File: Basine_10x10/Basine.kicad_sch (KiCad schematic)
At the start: 28 parts, among them J1 2060-451/998-404, J10 2060-451/998-404, J11 2060-451/998-404, J12 2060-451/998-404, J13 2060-451/998-404, J14 2060-451/998-404, J15 2060-451/998-404, J16 2060-451/998-404, J2 2060-451/998-404, J3 2060-451/998-404, J4 2060-451/998-404, J5 2060-451/998-404, J6 2060-451/998-404, J7 2060-451/998-404, J8 2060-451/998-404, J9 2060-451/998-404

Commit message: Basine_10x10 :
ajout ultrogothe
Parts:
- added JP10, JP11, JP12, JP13, JP14, JP15, JP16, JP5, JP6, JP7, JP8, JP9: SolderJumper_2_Open, Jumper:SolderJumper-2_P1.3mm_Open_TrianglePad1.0x1.5mm, symbol Jumper:SolderJumper_2_Open
- added TP1, TP10, TP11, TP12, TP2, TP3, TP4, TP5, TP6, TP7, TP8, TP9: TestPoint, Chimere_comps:Pastille, symbol Connector:TestPoint
- added U2: ~, symbol Chimere_mods:Ultrogothe
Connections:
- net 0V: now also U2.19 (0V)
- net 3V3: now also U2.20 (3V3)
- net 5V: now also U2.21 (5V)
- net at U7.4 (IO_i): now also JP7.2 (B), TP3.1
- net at U12.4 (IO_i): now also JP12.2 (B), TP8.1
- net at U9.4 (IO_i): now also JP9.2 (B), TP5.1
- net at U5.4 (IO_i): now also JP5.2 (B), TP1.1
- net at U10.4 (IO_i): now also JP10.2 (B), TP6.1
- net at U13.4 (IO_i): now also JP13.2 (B), TP9.1
- net at U6.4 (IO_i): now also JP6.2 (B), TP2.1
- net at U14.4 (IO_i): now also JP14.2 (B), TP10.1
- net at U8.4 (IO_i): now also JP8.2 (B), TP4.1
- net at U16.4 (IO_i): now also JP16.2 (B), TP12.1
- net at U15.4 (IO_i): now also JP15.2 (B), TP11.1
- net at U11.4 (IO_i): now also JP11.2 (B), TP7.1
- no-connect marks 0 -> 10
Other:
- removed sheet s_ALIM_3V3
- note removed: "Ultrogothe"

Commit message: Basine_10x10
ajout symbole ultrogothe
ajout power flag sur 5V
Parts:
- added JP17, JP18: SolderJumper_2_Open, Jumper:SolderJumper-2_P1.3mm_Open_TrianglePad1.0x1.5mm, symbol Jumper:SolderJumper_2_Open
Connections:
- net CAN_RX: now also JP18.2 (B)
- net CAN_TX: now also JP17.2 (B)
- net B0: now reaches JP8.1 (A)
- net B0: now also U2.30 (B0)
- net at U2.14 (B8): now also JP18.1 (A)
- net at U2.15 (B9): now also JP17.1 (A)
- net A0: now reaches U2.22 (A0)
- net A0: now also JP16.1 (A)
- net A1: now reaches U2.23 (A1)
- net A1: now also JP15.1 (A)
- net A2: now reaches U2.24 (A2)
- net A2: now also JP14.1 (A)
- net A3: now reaches U2.25 (A3)
- net A3: now also JP13.1 (A)
- net A4: now reaches U2.26 (A4)
- net A4: now also JP12.1 (A)
- net A5: now reaches U2.27 (A5)
- net A5: now also JP11.1 (A)
- net A6: now reaches U2.28 (A6)
- net A6: now also JP10.1 (A)
- net A7: now reaches U2.29 (A7)
- net A7: now also JP9.1 (A)
- net B1: now reaches U2.31 (B1)
- net B1: now also JP7.1 (A)
- net B2: now reaches U2.32 (B2)
- net B2: now also JP6.1 (A)
- net B10: now reaches U2.33 (B10)
- net B10: now also JP5.1 (A)
- no-connect marks 10 -> 31
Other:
- moved on the sheet: J1, J2, J3, J4, U2

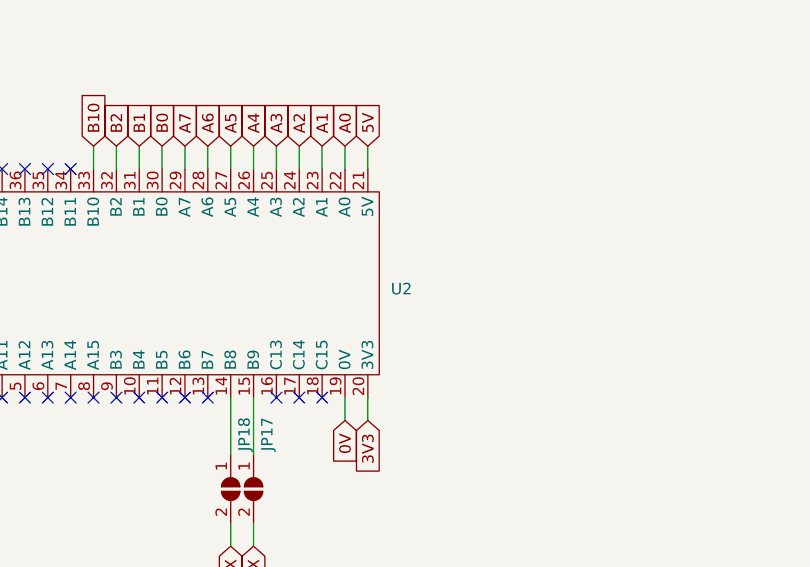
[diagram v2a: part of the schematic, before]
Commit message: 10x10
 ajout empreinte ultrogothe
placement ultrogothe et un peu alim 5V
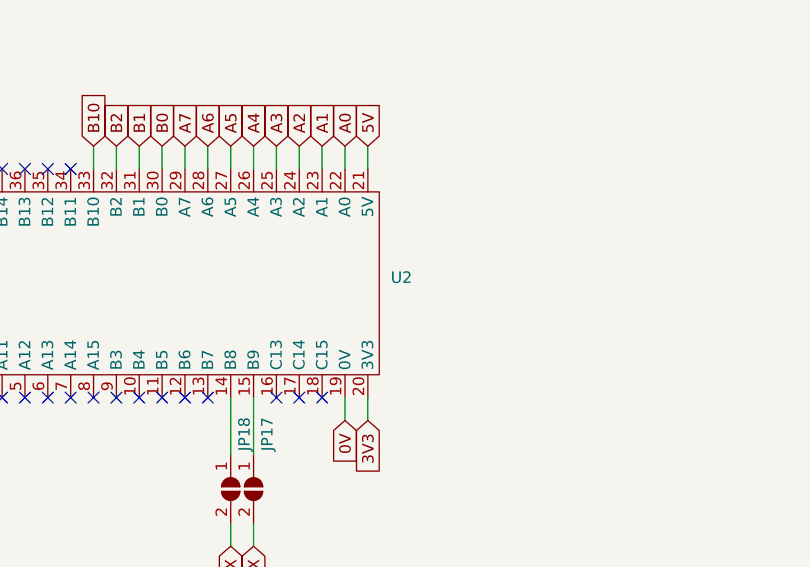
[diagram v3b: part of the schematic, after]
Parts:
- U2: footprint (none) -> Chimere_mods:Ultrogothe
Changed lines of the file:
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@@
 		(fields_autoplaced yes)
 		(property "Reference" "U2"
-			(at 147.32 140.3351 90)
+			(at 147.32 139.0649 90)
 			(effects
 				(font
@@
 		)
 		(property "Value" "~"
-			(at 147.32 138.43 90)
+			(at 147.32 140.97 90)
 			(effects
 				(font
@@
 			)
 		)
-		(property "Footprint" ""
+		(property "Footprint" "Chimere_mods:Ultrogothe"
 			(at 120.65 124.46 0)
 			(effects

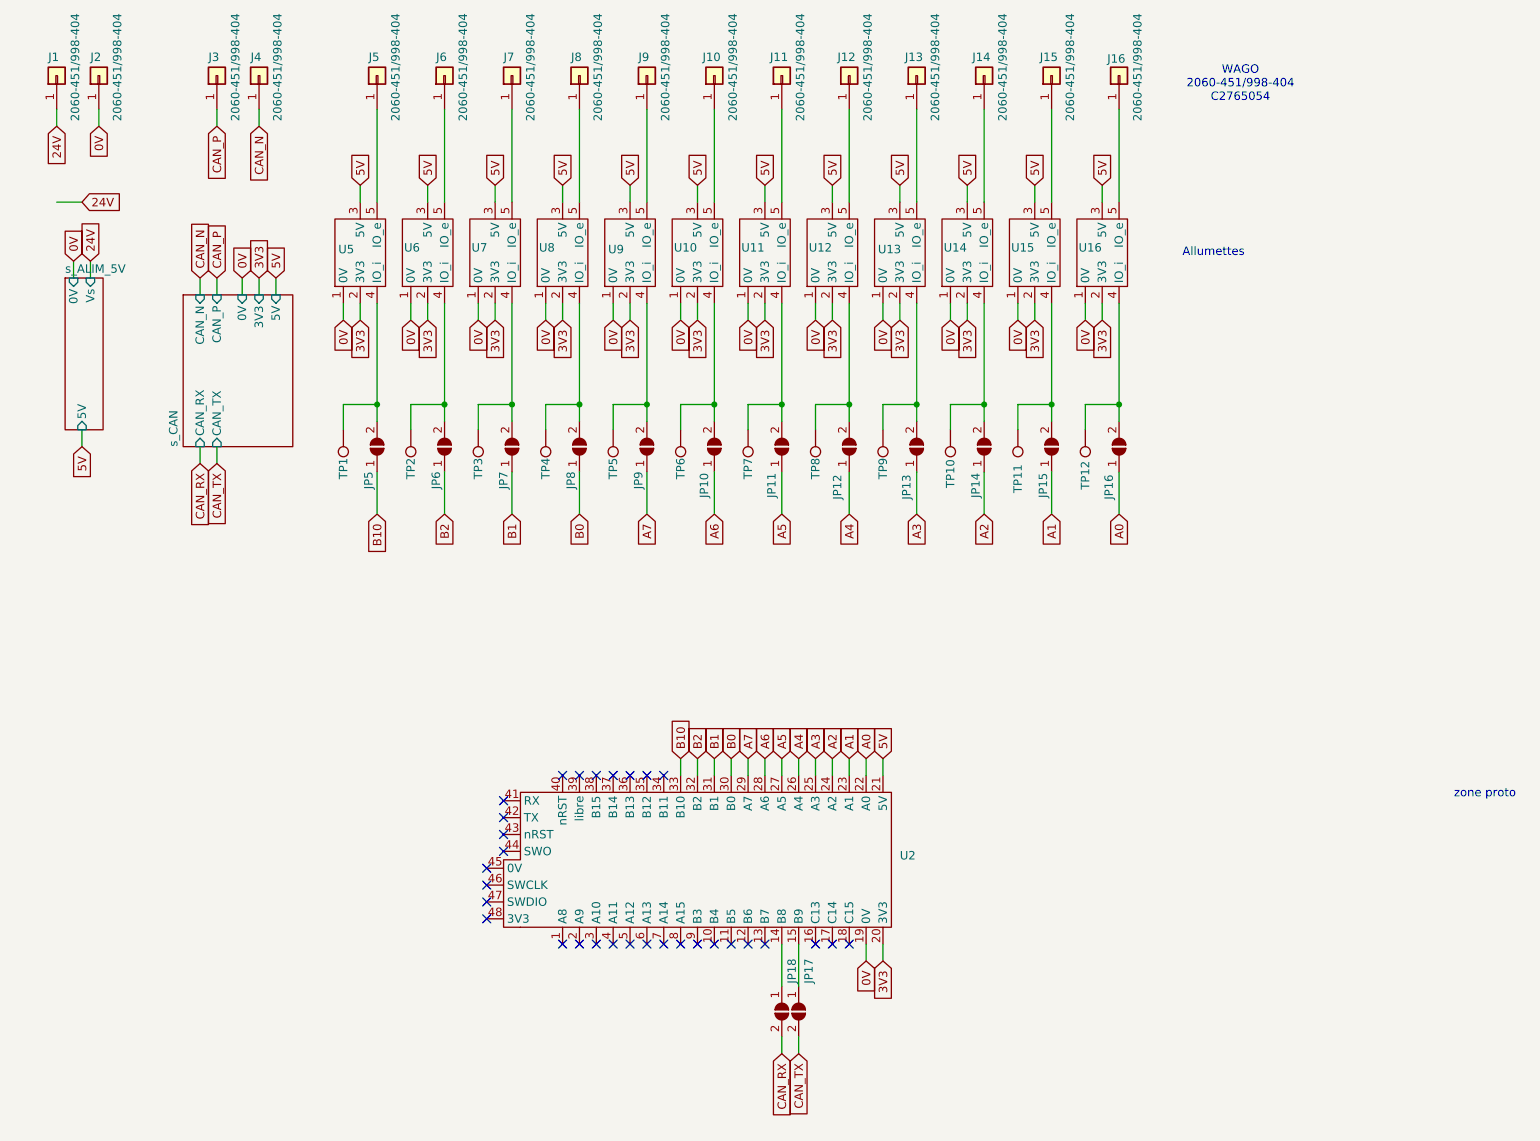
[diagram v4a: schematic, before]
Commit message: 10x10
alim 5V ok
placement et routage ok
reste vias à placer
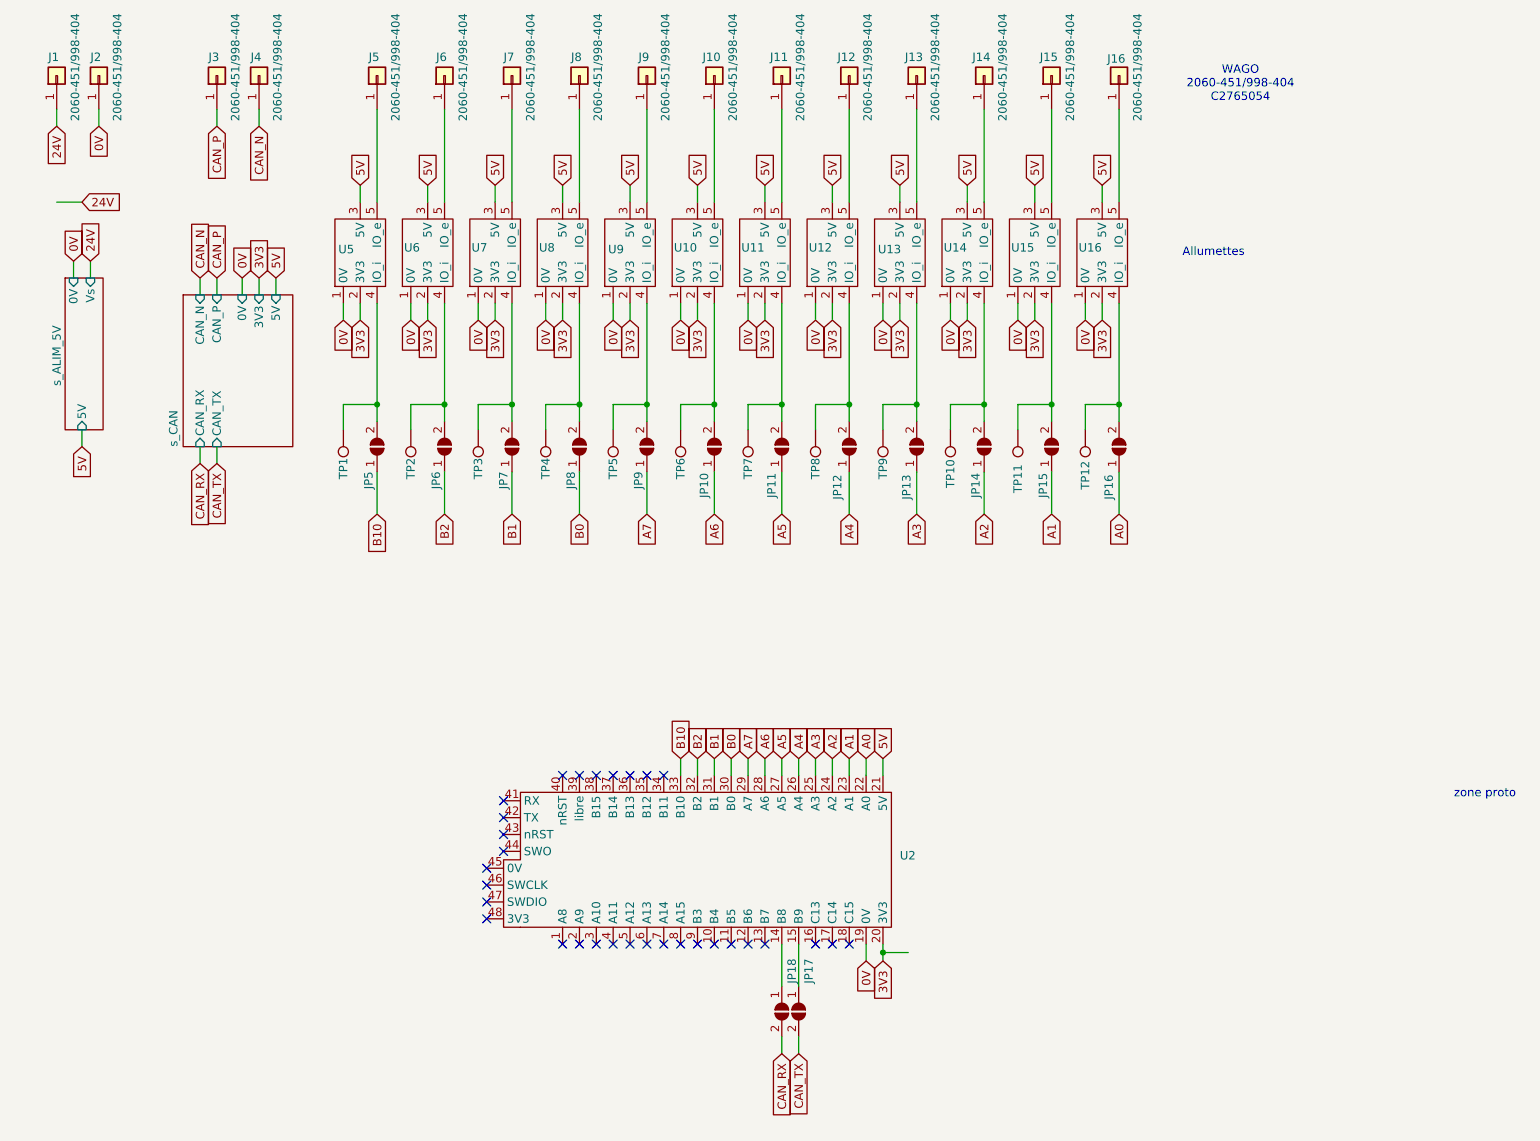
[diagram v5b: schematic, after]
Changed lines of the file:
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@@
 	)
 	(junction
+		(at 144.78 153.67)
+		(diameter 0)
+		(color 0 0 0 0)
+	)
+	(junction
 		(at 170.18 71.12)
 		(diameter 0)
@@
 	(wire
 		(pts
+			(xy 144.78 153.67) (xy 148.59 153.67)
+		)
+		(stroke
+			(width 0)
+			(type default)
+		)
+	)
+	(wire
+		(pts
 			(xy 48.26 52.07) (xy 48.26 54.61)
 		)
@@
 	(wire
 		(pts
+			(xy 144.78 153.67) (xy 144.78 152.4)
+		)
+		(stroke
+			(width 0)
+			(type default)
+		)
+	)
+	(wire
+		(pts
 			(xy 134.62 71.12) (xy 139.7 71.12)
 		)
@@
 	(wire
 		(pts
-			(xy 144.78 154.94) (xy 144.78 152.4)
+			(xy 144.78 154.94) (xy 144.78 153.67)
 		)
 		(stroke
@@
 	(netclass_flag ""
 		(length 2.54)
+		(shape round)
+		(at 148.59 153.67 0)
+		(fields_autoplaced yes)
+		(effects
+			(font
+				(size 1.27 1.27)
+			)
+			(justify left bottom)
+		)
+		(property "Netclass" "alim"
+			(at 149.2885 151.13 0)
+			(effects
+				(font
+					(size 1.27 1.27)
+					(italic yes)
+				)
+				(justify left)
+			)
+		)
+	)
+	(netclass_flag ""
+		(length 2.54)
 		(shape dot)
 		(at 88.9 31.75 90)
@@
 		)
 		(property "Sheetname" "s_ALIM_5V"
-			(at 21.59 51.435 0)
+			(at 21.082 68.326 90)
 			(effects
 				(font

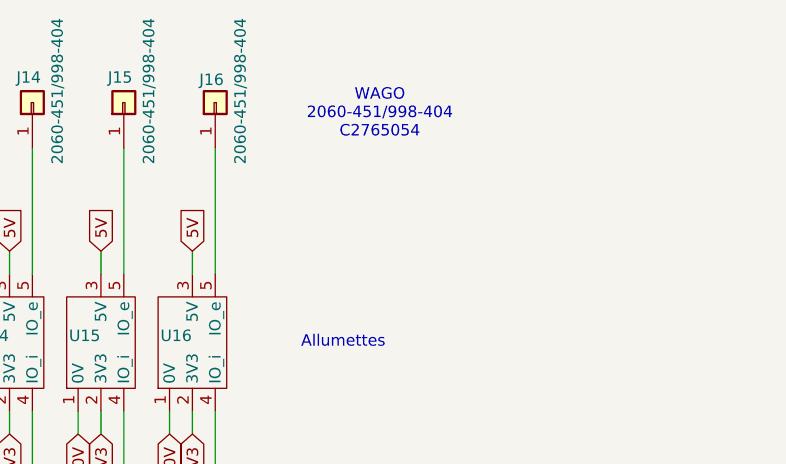
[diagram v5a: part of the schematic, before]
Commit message: 10x10
tentative de fabrication
pénurie spring clamp à gérer
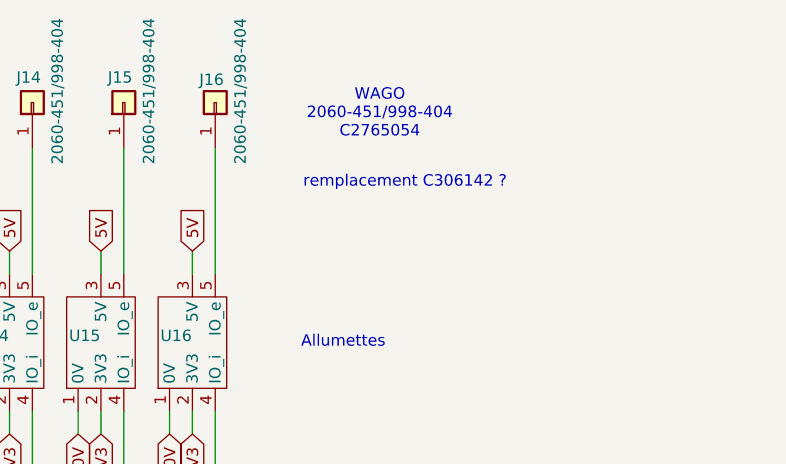
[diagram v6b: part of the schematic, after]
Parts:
- TP1, TP10, TP11, TP12, TP2, TP3, TP4, TP5, TP6, TP7, TP8, TP9, U10, U11, U12, U13, U14, U15, U16, U2, U5, U6, U7, U8, U9: now left out of the parts list
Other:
- note added: "remplacement C306142 ?"
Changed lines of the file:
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@@
 		)
 	)
+	(text "remplacement C306142 ?"
+		(exclude_from_sim no)
+		(at 201.422 30.48 0)
+		(effects
+			(font
+				(size 1.27 1.27)
+			)
+		)
+	)
 	(text "WAGO\n2060-451/998-404\nC2765054"
 		(exclude_from_sim no)
@@
 		(unit 1)
 		(exclude_from_sim no)
-		(in_bom yes)
+		(in_bom no)
 		(on_board yes)
 		(dnp no)
@@
 		(unit 1)
 		(exclude_from_sim no)
-		(in_bom yes)
+		(in_bom no)
 		(on_board yes)
 		(dnp no)
@@
 		(unit 1)
 		(exclude_from_sim no)
-		(in_bom yes)
+		(in_bom no)
 		(on_board yes)
 		(dnp no)
@@
 		(unit 1)
 		(exclude_from_sim no)
-		(in_bom yes)
+		(in_bom no)
 		(on_board yes)
 		(dnp no)
@@
 		(unit 1)
 		(exclude_from_sim no)
-		(in_bom yes)
+		(in_bom no)
 		(on_board yes)
 		(dnp no)
@@
 		(unit 1)
 		(exclude_from_sim no)
-		(in_bom yes)
+		(in_bom no)
 		(on_board yes)
 		(dnp no)
@@
 		(unit 1)
 		(exclude_from_sim no)
-		(in_bom yes)
+		(in_bom no)
 		(on_board yes)
 		(dnp no)
@@
 		(unit 1)
 		(exclude_from_sim no)
-		(in_bom yes)
+		(in_bom no)
 		(on_board yes)
 		(dnp no)
@@
 		(unit 1)
 		(exclude_from_sim no)
-		(in_bom yes)
+		(in_bom no)
 		(on_board yes)
 		(dnp no)
@@
 		(unit 1)
 		(exclude_from_sim no)
-		(in_bom yes)
+		(in_bom no)
 		(on_board yes)
 		(dnp no)
@@
 		(unit 1)
 		(exclude_from_sim no)
-		(in_bom yes)
+		(in_bom no)
 		(on_board yes)
 		(dnp no)
@@
 		(unit 1)
 		(exclude_from_sim no)
-		(in_bom yes)
+		(in_bom no)
 		(on_board yes)
 		(dnp no)
@@
 		(unit 1)
 		(exclude_from_sim no)
-		(in_bom yes)
+		(in_bom no)
 		(on_board yes)
 		(dnp no)
@@
 		(unit 1)
 		(exclude_from_sim no)
-		(in_bom yes)
+		(in_bom no)
 		(on_board yes)
 		(dnp no)
@@
 		(unit 1)
 		(exclude_from_sim no)
-		(in_bom yes)
+		(in_bom no)
 		(on_board yes)
 		(dnp no)
@@
 		(unit 1)
 		(exclude_from_sim no)
-		(in_bom yes)
+		(in_bom no)
 		(on_board yes)
 		(dnp no)
@@
 		(unit 1)
 		(exclude_from_sim no)
-		(in_bom yes)
+		(in_bom no)
 		(on_board yes)
 		(dnp no)
@@
 		(unit 1)
 		(exclude_from_sim no)
-		(in_bom yes)
+		(in_bom no)
 		(on_board yes)
 		(dnp no)
@@
 		(unit 1)
 		(exclude_from_sim no)
-		(in_bom yes)
+		(in_bom no)
 		(on_board yes)
 		(dnp no)
@@
 		(unit 1)
 		(exclude_from_sim no)
-		(in_bom yes)
+		(in_bom no)
 		(on_board yes)
 		(dnp no)
@@
 		(unit 1)
 		(exclude_from_sim no)
-		(in_bom yes)
+		(in_bom no)
 		(on_board yes)
 		(dnp no)
@@
 		(unit 1)
 		(exclude_from_sim no)
-		(in_bom yes)
+		(in_bom no)
 		(on_board yes)
 		(dnp no)
@@
 		(unit 1)
 		(exclude_from_sim no)
-		(in_bom yes)
+		(in_bom no)
 		(on_board yes)
 		(dnp no)
@@
 		(unit 1)
 		(exclude_from_sim no)
-		(in_bom yes)
+		(in_bom no)
 		(on_board yes)
 		(dnp no)
@@
 		(unit 1)
 		(exclude_from_sim no)
-		(in_bom yes)
+		(in_bom no)
 		(on_board yes)
 		(dnp no)

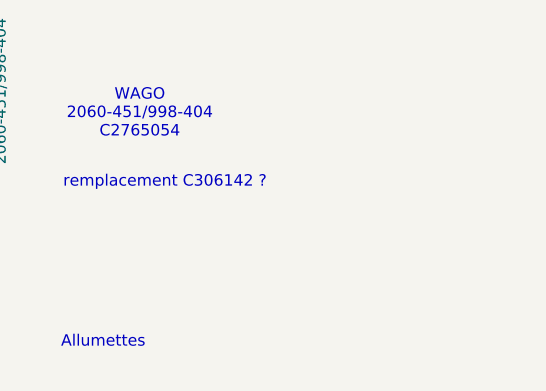
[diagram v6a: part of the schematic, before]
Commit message: 10x10
ajout ref traversante de wago
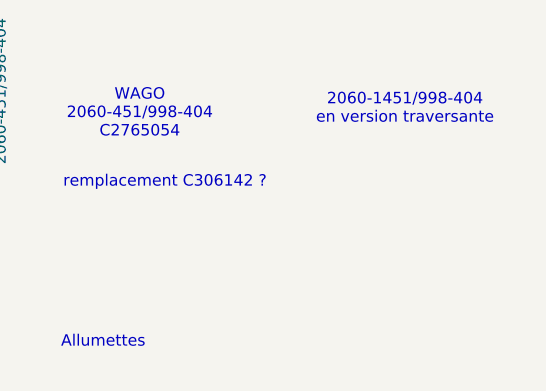
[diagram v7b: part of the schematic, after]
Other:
- note added: "2060-1451/998-404 en version traversante"
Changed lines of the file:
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@@
+		)
+	)
+	(text "2060-1451/998-404\nen version traversante"
+		(exclude_from_sim no)
+		(at 228.092 22.352 0)
+		(effects
+			(font
+				(size 1.27 1.27)
+			)
 		)
 	)
